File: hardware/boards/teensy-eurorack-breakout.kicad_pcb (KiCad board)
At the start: 2 copper layers, 110.5 x 111.1 mm, 74 parts, among them J1 Conn_01x08, SW1 Rotary_Encoder_Switch, SW2 Rotary_Encoder_Switch, SW3 Rotary_Encoder_Switch, U2 AD5754BREZ, U3 AD5754BREZ, U5 MCP1700-2502E, U6 AD7606BSTZ, U7 6N138

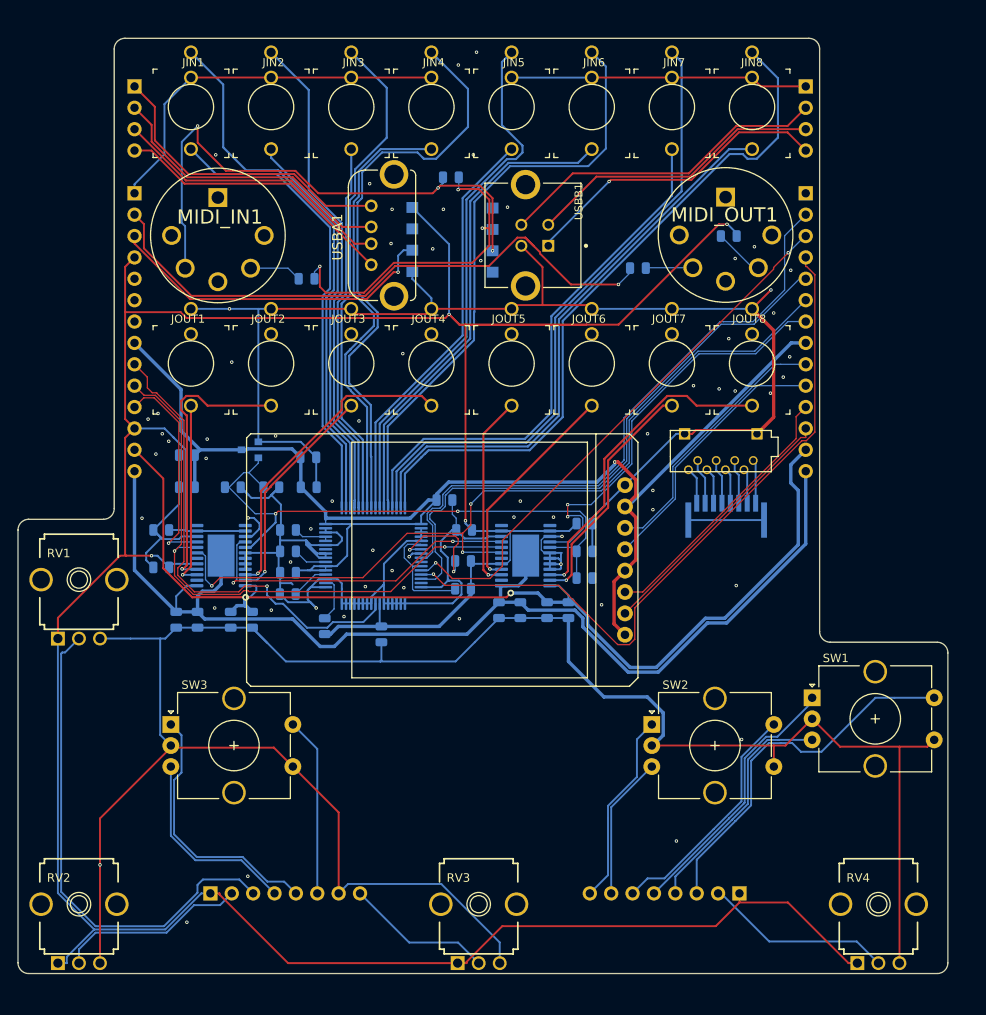
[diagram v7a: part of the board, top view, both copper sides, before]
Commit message: fix schematic errors and change breakout to 4 layer board
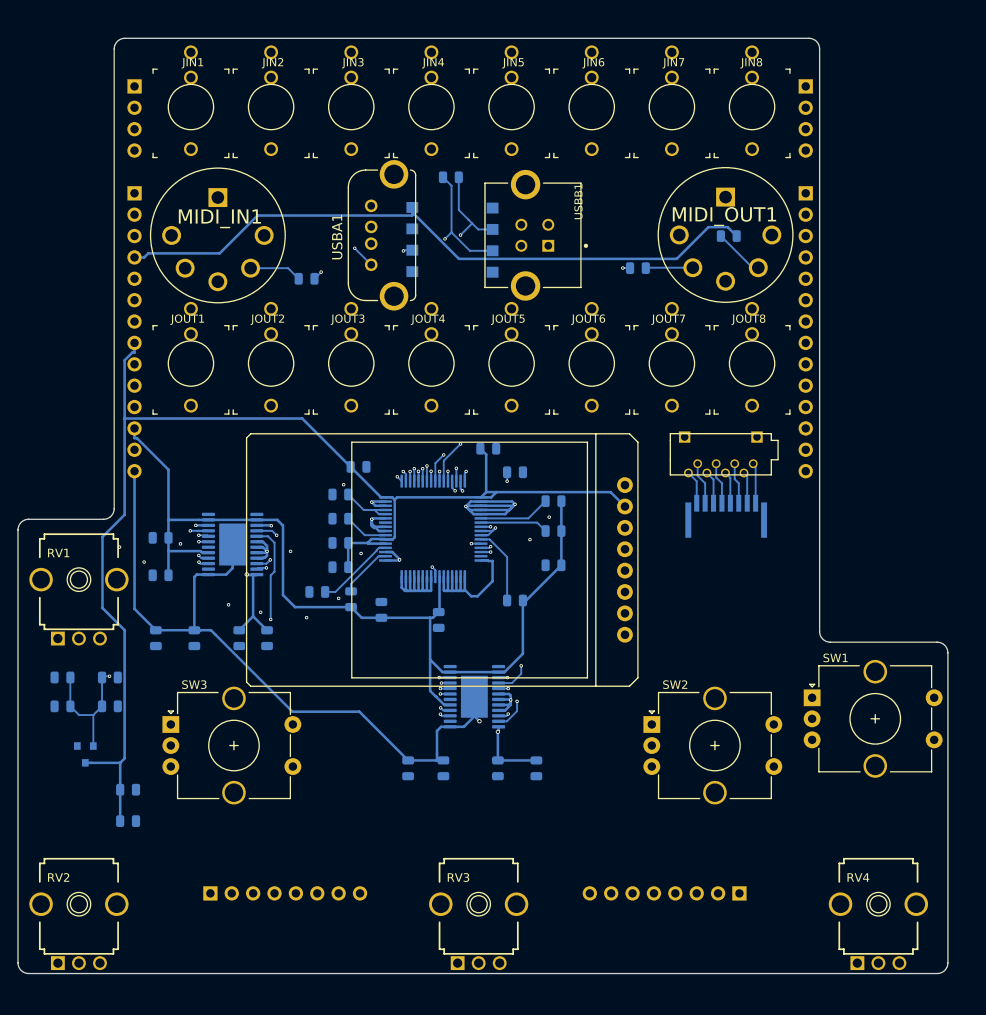
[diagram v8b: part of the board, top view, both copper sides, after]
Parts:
- added R1: 4.7k, Resistor_SMD:R_0805_2012Metric, B.Cu at (142.2, 107.7)
- added R2: 4.7k, Resistor_SMD:R_0805_2012Metric, B.Cu at (142.2, 92.5)
- moved C39 64.7 mm to (88.5, 120.3), turned to 180 degrees
- moved C37 63.1 mm to (88.5, 116.8), turned to 180 degrees
- moved C27 44.0 mm to (96.3, 133.9), turned to 180 degrees
- moved U5 41.1 mm to (91.2, 126.0), turned to 270 degrees
- moved C28 36.6 mm to (96.3, 130.2), turned to 180 degrees
- moved C30 29.9 mm to (94.1, 120.3)
- moved C29 29.6 mm to (94.1, 116.8)
- moved C33 23.0 mm to (129.5, 127.6)
- moved C20 20.8 mm to (133.2, 110.0), turned to 270 degrees
- moved C23 20.6 mm to (140.2, 127.6)
- moved C32 19.9 mm to (133.7, 127.6)
- moved C19 18.8 mm to (144.8, 127.6)
- moved U3 17.8 mm to (137.4, 119.1)
- moved R5 15.0 mm to (146.8, 95.9)
- moved C24 11.4 mm to (146.8, 103.5)
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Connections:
- U6 pad 11: Net-(R5-Pad2) -> Net-(R1-Pad2)
- U6 pad 8: GND -> Net-(R2-Pad1)
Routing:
- net GND: track 661.7 -> 97.8 mm, vias 65 -> 22
- net +5V: track 165.2 -> 198.0 mm, vias 1 -> 0
- net /ADC_CS: track 84.2 -> 52.9 mm
- net +3V3: track 417.7 -> 391.8 mm, vias 4 -> 0
- net /P1: track 59.2 -> 38.9 mm
- net /VOUT5: track 23.3 -> 42.6 mm
- net /VGND8: track 84.1 -> 65.1 mm, vias 0 -> 1
- net Net-(D1-Pad2): track 66.0 -> 47.3 mm, vias 3 -> 1
- net /VOUT6: track 26.1 -> 44.6 mm
- net /ADC_BUSY: track 70.3 -> 52.0 mm, vias 0 -> 1
- net /VOUT7: track 28.5 -> 46.6 mm
- net /VGND4: track 69.9 -> 51.9 mm, vias 0 -> 1
- net /ADC_CONVST: track 74.2 -> 57.9 mm, vias 0 -> 1
- net /VGND7: track 75.7 -> 61.6 mm, vias 0 -> 1
- net /VIN4: track 53.5 -> 40.1 mm, vias 0 -> 1
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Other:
- copper layers 2 -> 4
- net class Default: trace_width 0.1524 -> 0.2286; via_dia 0.8 -> 0.4064; via_drill 0.4 -> 0.2032
- net class PWR added: clearance 0.1524, trace_width 0.3048, via_dia 0.508, via_drill 0.3048
